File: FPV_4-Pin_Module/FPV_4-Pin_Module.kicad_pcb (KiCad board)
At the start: 2 copper layers, 33.5 x 25.2 mm, 3 parts, among them J2 Conn_01x10_Socket, J3 Conn_01x10_Socket

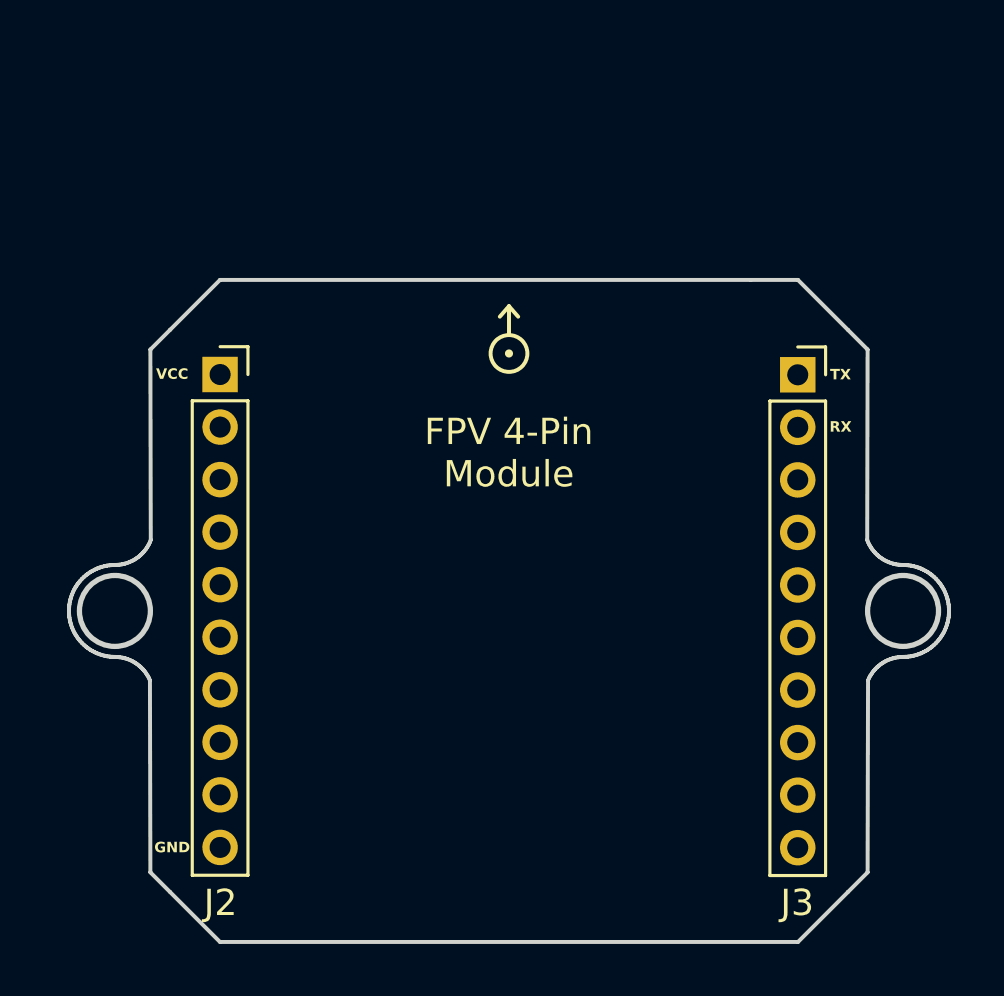
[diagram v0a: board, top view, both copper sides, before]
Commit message: Adding FPV 4-pin interface module
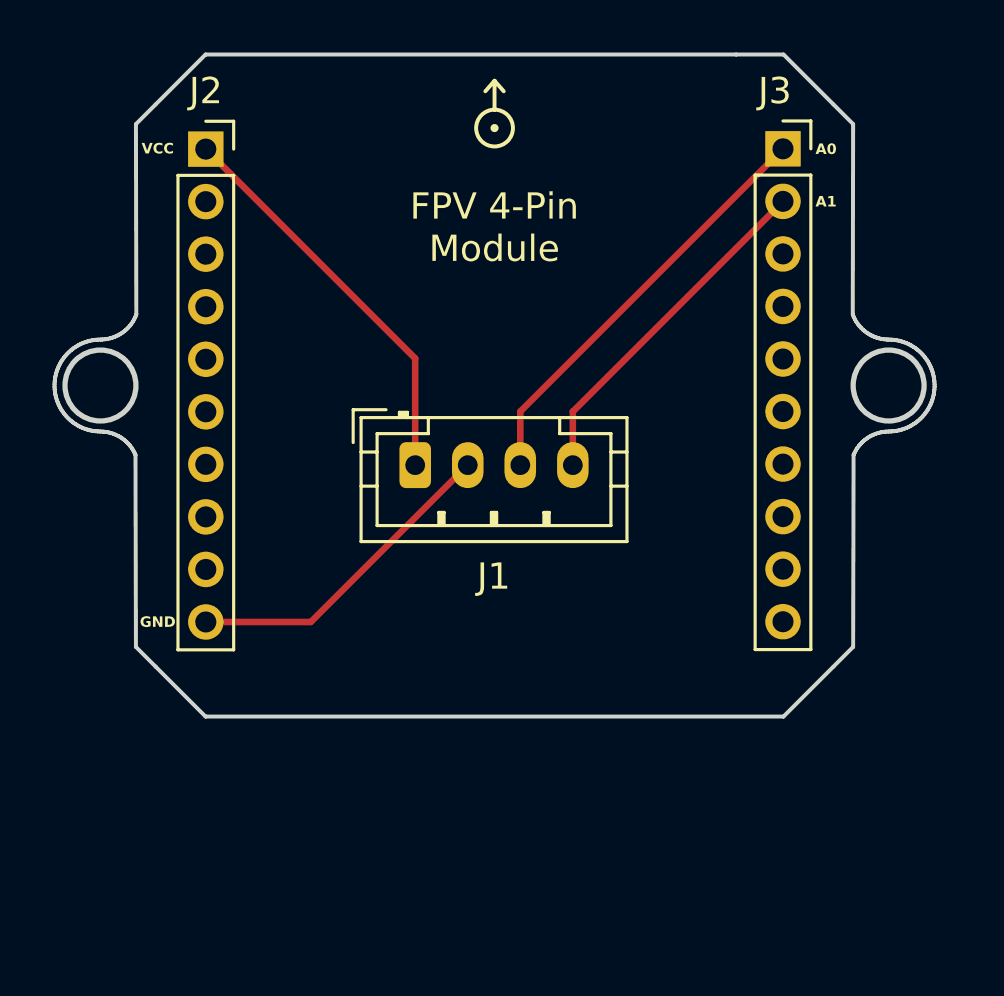
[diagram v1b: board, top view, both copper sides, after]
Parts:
- added J1: Conn_01x04_Socket, Connector_JST:JST_PH_B4B-PH-K_1x04_P2.00mm_Vertical, F.Cu at (146.3, 83.3)
- moved J3 8.62 mm to (160.3, 71.3)
- moved J2 8.60 mm to (138.3, 71.3)
- moved EXP_ORIENTATION 8.60 mm to (149.3, 70.5)
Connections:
- J2 pad 1: (no net) -> Net-(J1-Pin_1)
- J2 pad 10: (no net) -> Net-(J1-Pin_2)
- J2 pad 2: (no net) -> unconnected-(J2-Pin_2-Pad2)
- J2 pad 3: (no net) -> unconnected-(J2-Pin_3-Pad3)
- J2 pad 4: (no net) -> unconnected-(J2-Pin_4-Pad4)
- J2 pad 5: (no net) -> unconnected-(J2-Pin_5-Pad5)
- J2 pad 6: (no net) -> unconnected-(J2-Pin_6-Pad6)
- J2 pad 7: (no net) -> unconnected-(J2-Pin_7-Pad7)
- J2 pad 8: (no net) -> unconnected-(J2-Pin_8-Pad8)
- J2 pad 9: (no net) -> unconnected-(J2-Pin_9-Pad9)
- J3 pad 1: (no net) -> Net-(J1-Pin_3)
- J3 pad 10: (no net) -> unconnected-(J3-Pin_10-Pad10)
- J3 pad 2: (no net) -> Net-(J1-Pin_4)
- J3 pad 3: (no net) -> unconnected-(J3-Pin_3-Pad3)
- J3 pad 4: (no net) -> unconnected-(J3-Pin_4-Pad4)
- J3 pad 5: (no net) -> unconnected-(J3-Pin_5-Pad5)
- J3 pad 6: (no net) -> unconnected-(J3-Pin_6-Pad6)
- J3 pad 7: (no net) -> unconnected-(J3-Pin_7-Pad7)
- J3 pad 8: (no net) -> unconnected-(J3-Pin_8-Pad8)
- J3 pad 9: (no net) -> unconnected-(J3-Pin_9-Pad9)
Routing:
- net Net-(J1-Pin_3): track 0.00 -> 16.2 mm
- net Net-(J1-Pin_1): track 0.00 -> 15.3 mm
- net Net-(J1-Pin_4): track 0.00 -> 13.4 mm
- net Net-(J1-Pin_2): track 0.00 -> 12.4 mm
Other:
- board text added: "A0"
- board text added: "A1"
- board text removed: "RX"
- board text removed: "TX"
